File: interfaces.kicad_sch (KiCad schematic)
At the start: 36 parts, among them J4 1140084168, J5 0473460001, U1 TS3USB30EDGSR, U5 TS3USB30EDGSR, U6 FT234XD-R

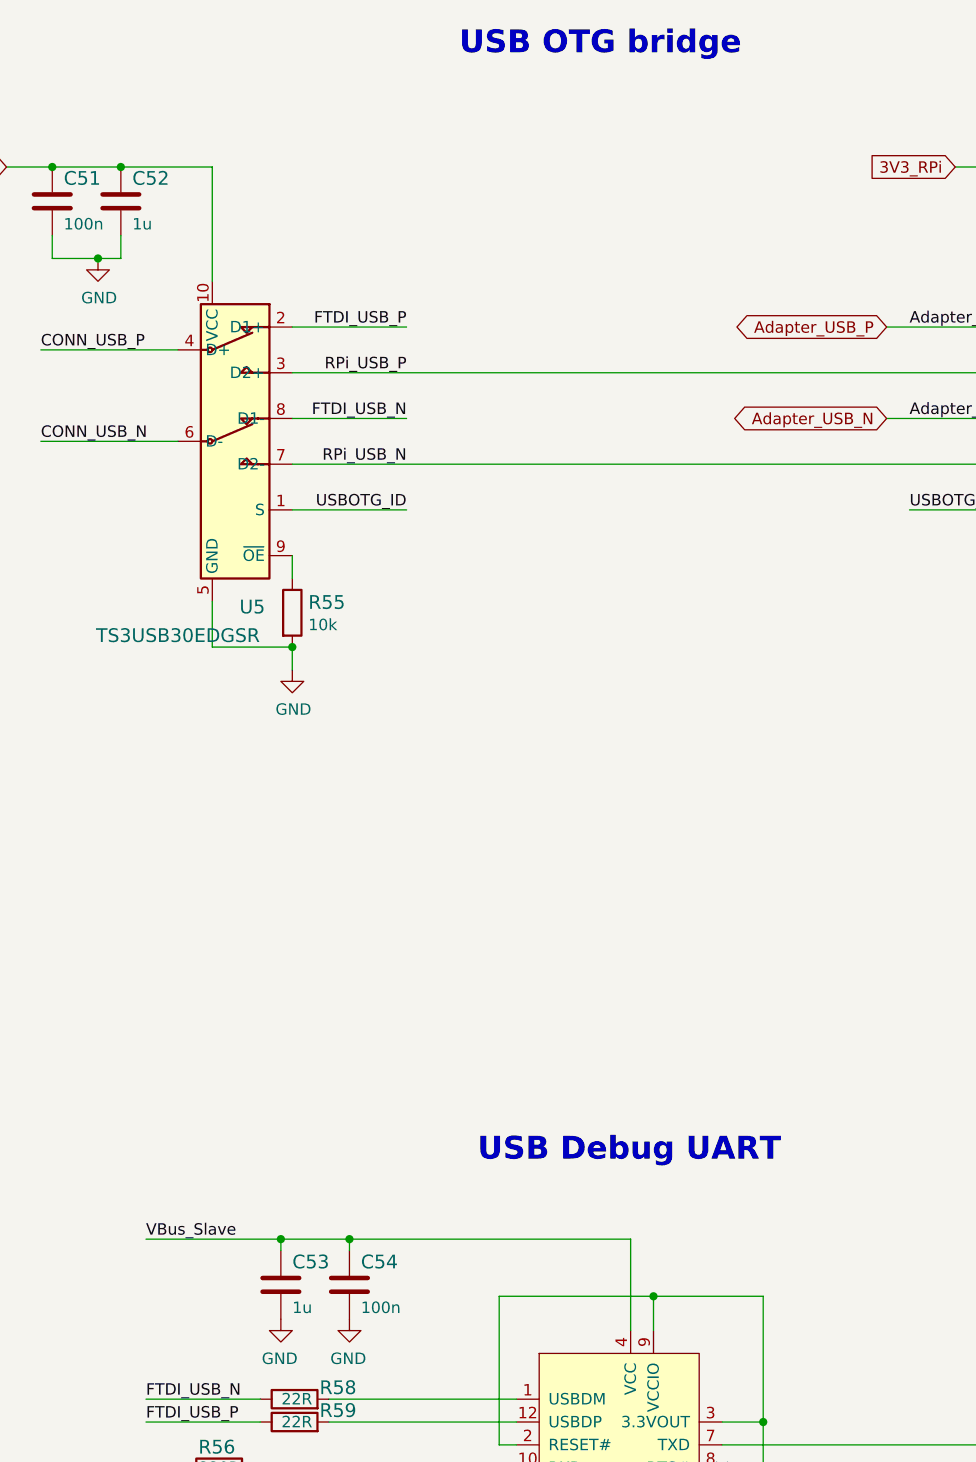
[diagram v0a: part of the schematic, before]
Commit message: Update C1,C2,C3 symbol and footprint
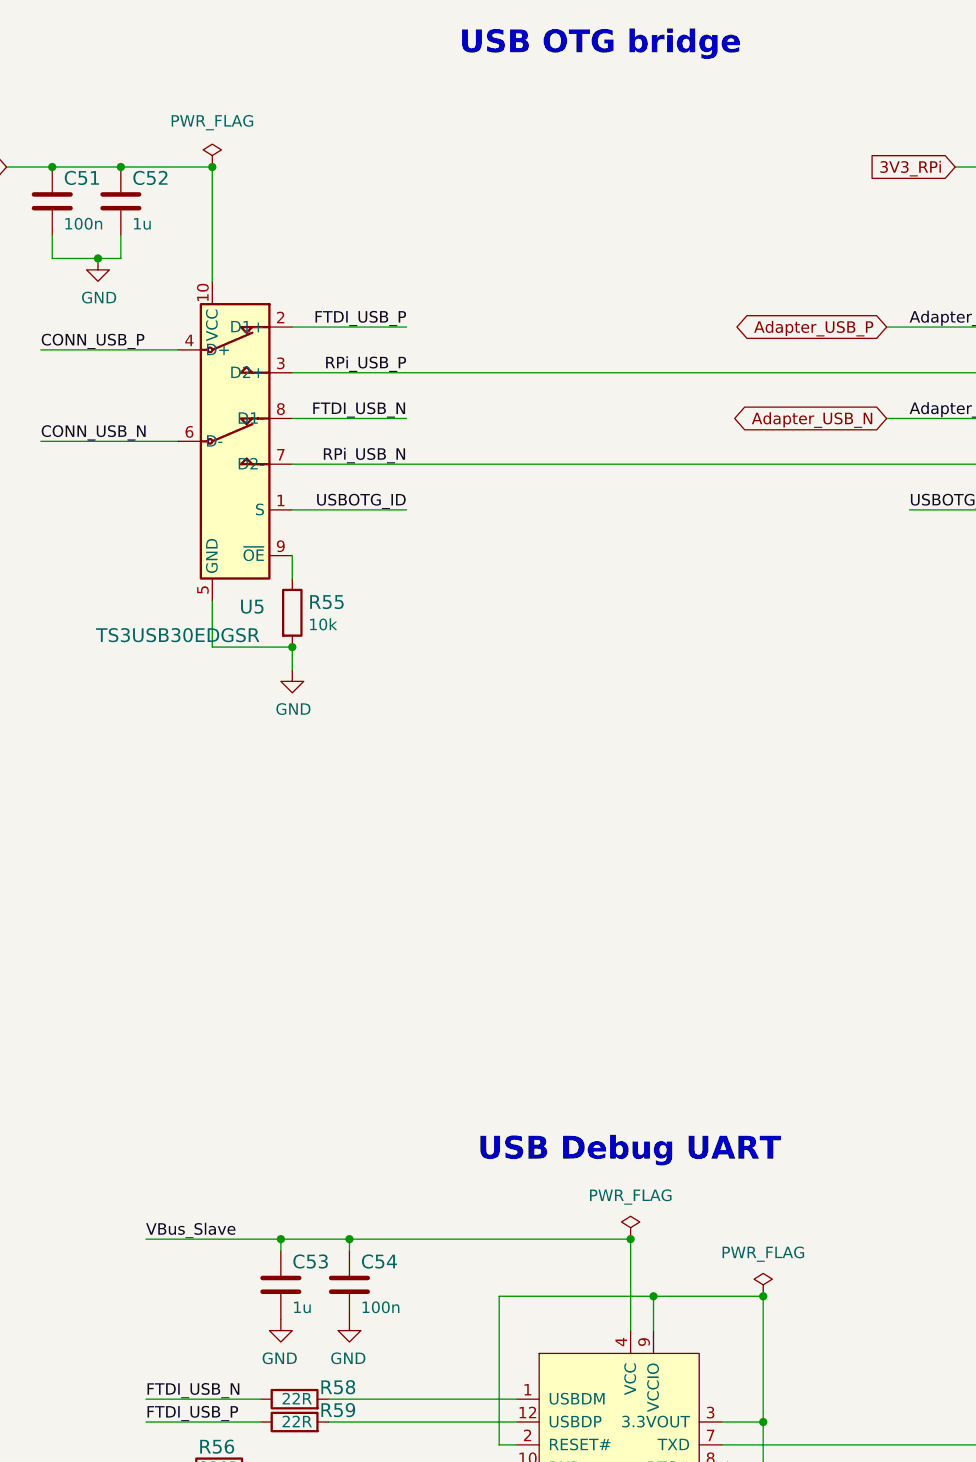
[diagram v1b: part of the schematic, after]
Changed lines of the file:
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@@
   (junction (at 45.466 188.976) (diameter 0) (color 0 0 0 0)
   )
+  (junction (at 232.41 48.26) (diameter 0) (color 0 0 0 0)
+  )
   (junction (at 50.546 178.816) (diameter 0) (color 0 0 0 0)
   )
@@
   (junction (at 111.506 205.486) (diameter 0) (color 0 0 0 0)
   )
+  (junction (at 293.624 173.736) (diameter 0) (color 0 0 0 0)
+  )
   (junction (at 79.756 63.5) (diameter 0) (color 0 0 0 0)
   )
@@
   (junction (at 281.432 173.736) (diameter 0) (color 0 0 0 0)
   )
+  (junction (at 278.892 167.386) (diameter 0) (color 0 0 0 0)
+  )
   (junction (at 74.676 188.976) (diameter 0) (color 0 0 0 0)
   )
@@
     (pin "2")
   )
+  (symbol (lib_id "antmicropower:PWR_FLAG") (at 293.624 173.736 0) (unit 1)
+    (in_bom yes) (on_board yes) (fields_autoplaced)
+    (property "Reference" "#FLG0103" (id 0) (at 293.624 171.831 0)
+      (effects (font (size 1.27 1.27)) hide)
+    )
+    (property "Value" "PWR_FLAG" (id 1) (at 293.624 168.91 0))
+    (property "Footprint" "" (id 2) (at 293.624 173.736 0)
+      (effects (font (size 1.27 1.27)) hide)
+    )
+    (property "Datasheet" "" (id 3) (at 293.624 173.736 0)
+      (effects (font (size 1.27 1.27)) hide)
+    )
+    (pin "1")
+  )
+  (symbol (lib_id "antmicropower:PWR_FLAG") (at 278.892 167.386 0) (unit 1)
+    (in_bom yes) (on_board yes) (fields_autoplaced)
+    (property "Reference" "#FLG0104" (id 0) (at 278.892 165.481 0)
+      (effects (font (size 1.27 1.27)) hide)
+    )
+    (property "Value" "PWR_FLAG" (id 1) (at 278.892 162.56 0))
+    (property "Footprint" "" (id 2) (at 278.892 167.386 0)
+      (effects (font (size 1.27 1.27)) hide)
+    )
+    (property "Datasheet" "" (id 3) (at 278.892 167.386 0)
+      (effects (font (size 1.27 1.27)) hide)
+    )
+    (pin "1")
+  )
+  (symbol (lib_id "antmicropower:PWR_FLAG") (at 232.41 48.26 0) (unit 1)
+    (in_bom yes) (on_board yes) (fields_autoplaced)
+    (property "Reference" "#FLG0102" (id 0) (at 232.41 46.355 0)
+      (effects (font (size 1.27 1.27)) hide)
+    )
+    (property "Value" "PWR_FLAG" (id 1) (at 232.41 43.18 0))
+    (property "Footprint" "" (id 2) (at 232.41 48.26 0)
+      (effects (font (size 1.27 1.27)) hide)
+    )
+    (property "Datasheet" "" (id 3) (at 232.41 48.26 0)
+      (effects (font (size 1.27 1.27)) hide)
+    )
+    (pin "1")
+  )
 )

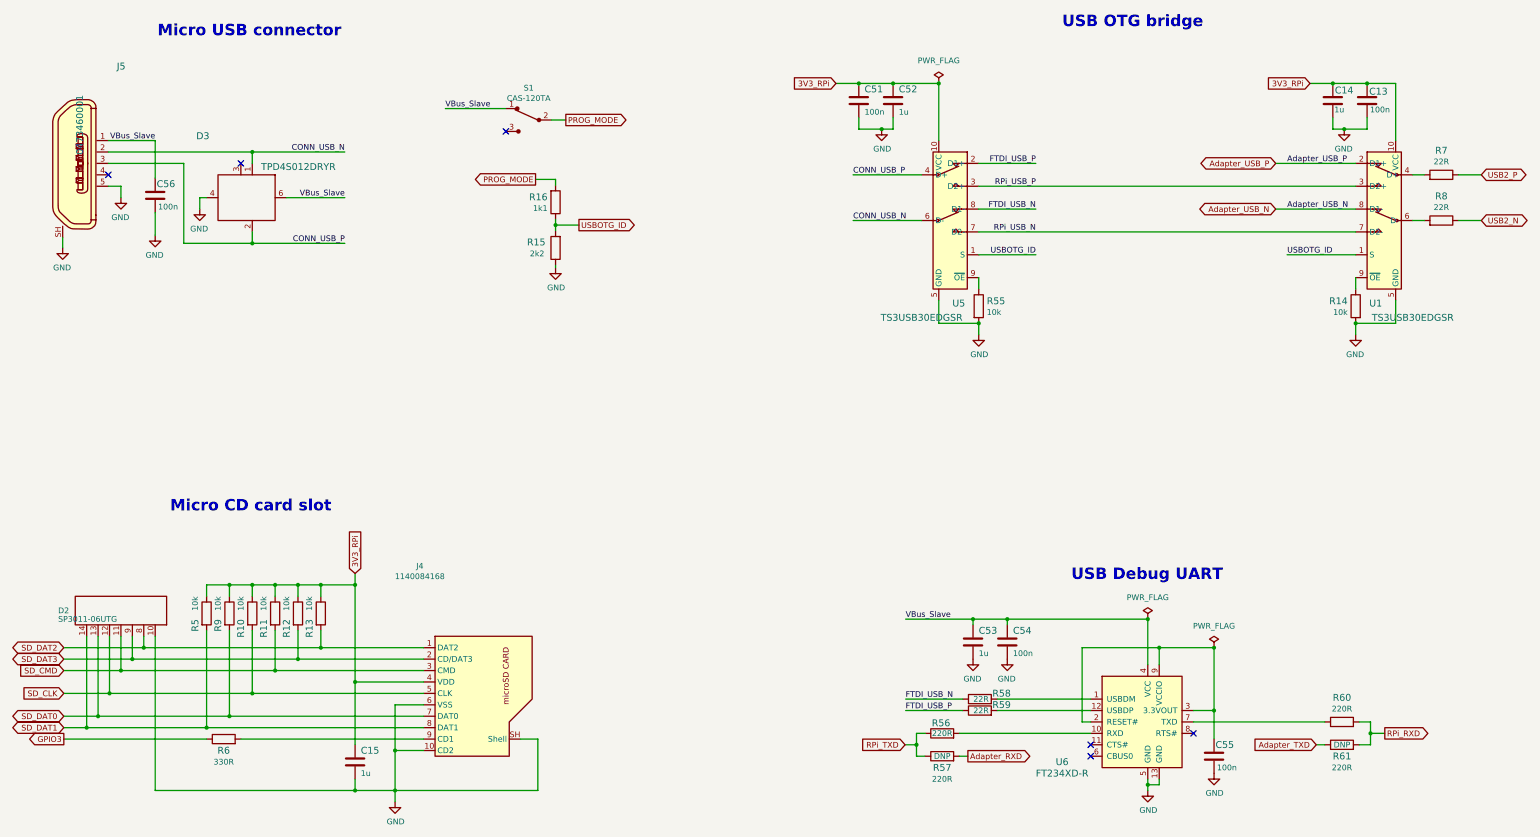
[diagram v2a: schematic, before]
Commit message: Update C13, C17, C21, C37, C51, C54, C55, C56 symbol and footprint
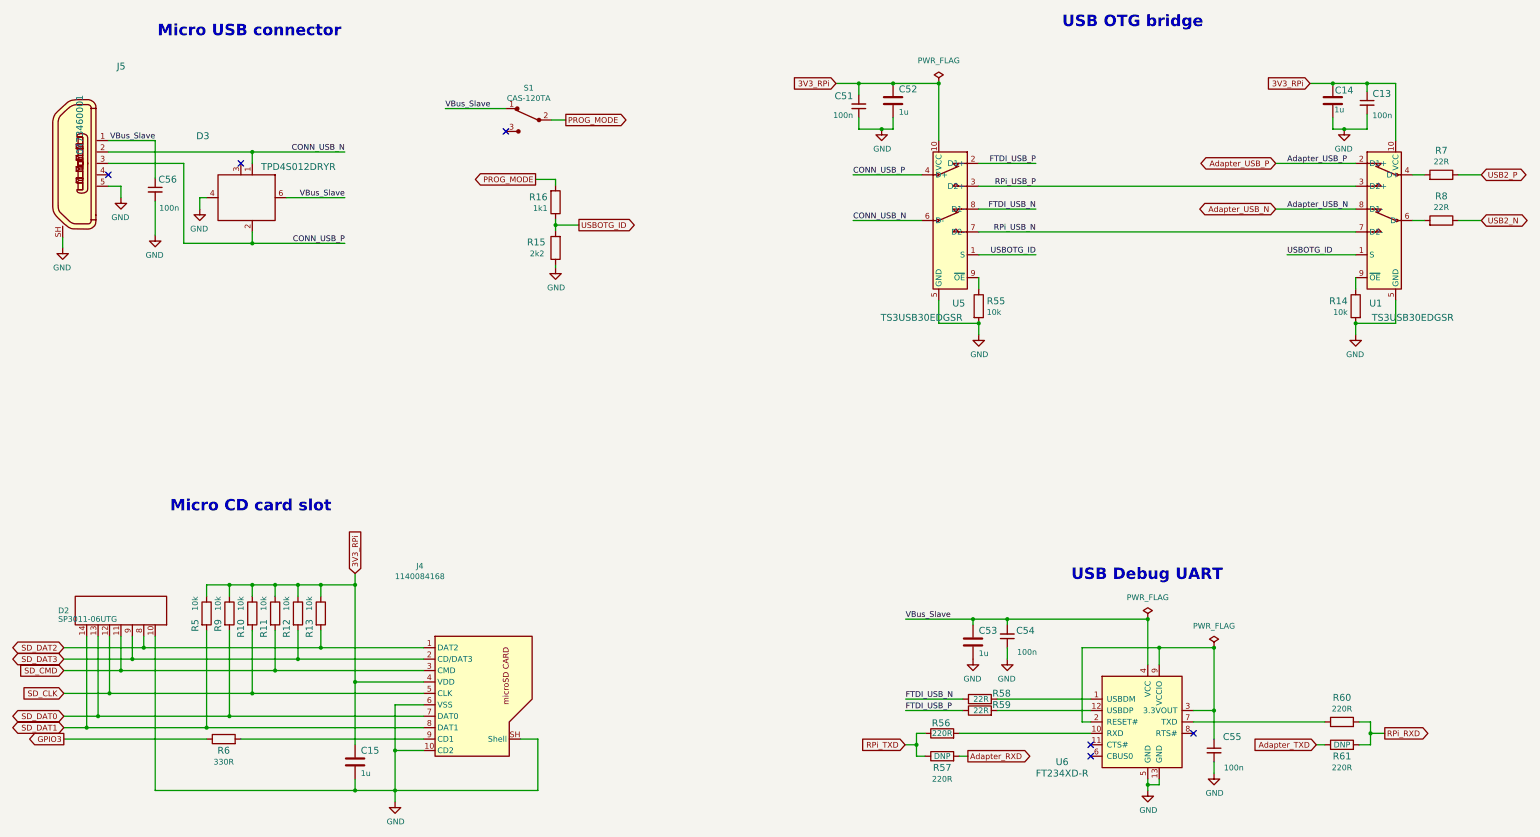
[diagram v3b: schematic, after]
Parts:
- C13, C51, C54, C55, C56: footprint scalenode-cm4-baseboard-footprints:0402-cap -> antmicro-footprints:C_0402_1005Metric; symbol scalenode-cm4-baseboard:C_100n_0402 -> antmicroCapacitors0402:C_100n_0402; Author (none) -> Antmicro; Dielectric (none) -> X5R; License (none) -> Apache-2.0; MPN 0402X104K6R3CT -> GRM155R61H104KE14D; Manufacturer Walsin -> Murata; Voltage (none) -> 50V
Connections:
- net 3V3_RPi: now also C51.2; no longer C51.1
- net GND: now also C51.1, C54.1; no longer C51.2, C54.2
- net VBus_Slave: now also C54.2; no longer C54.1
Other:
- moved on the sheet: C13, C51, C54, C55, C56

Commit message: Update C16, C18, C19 symbol and footprint
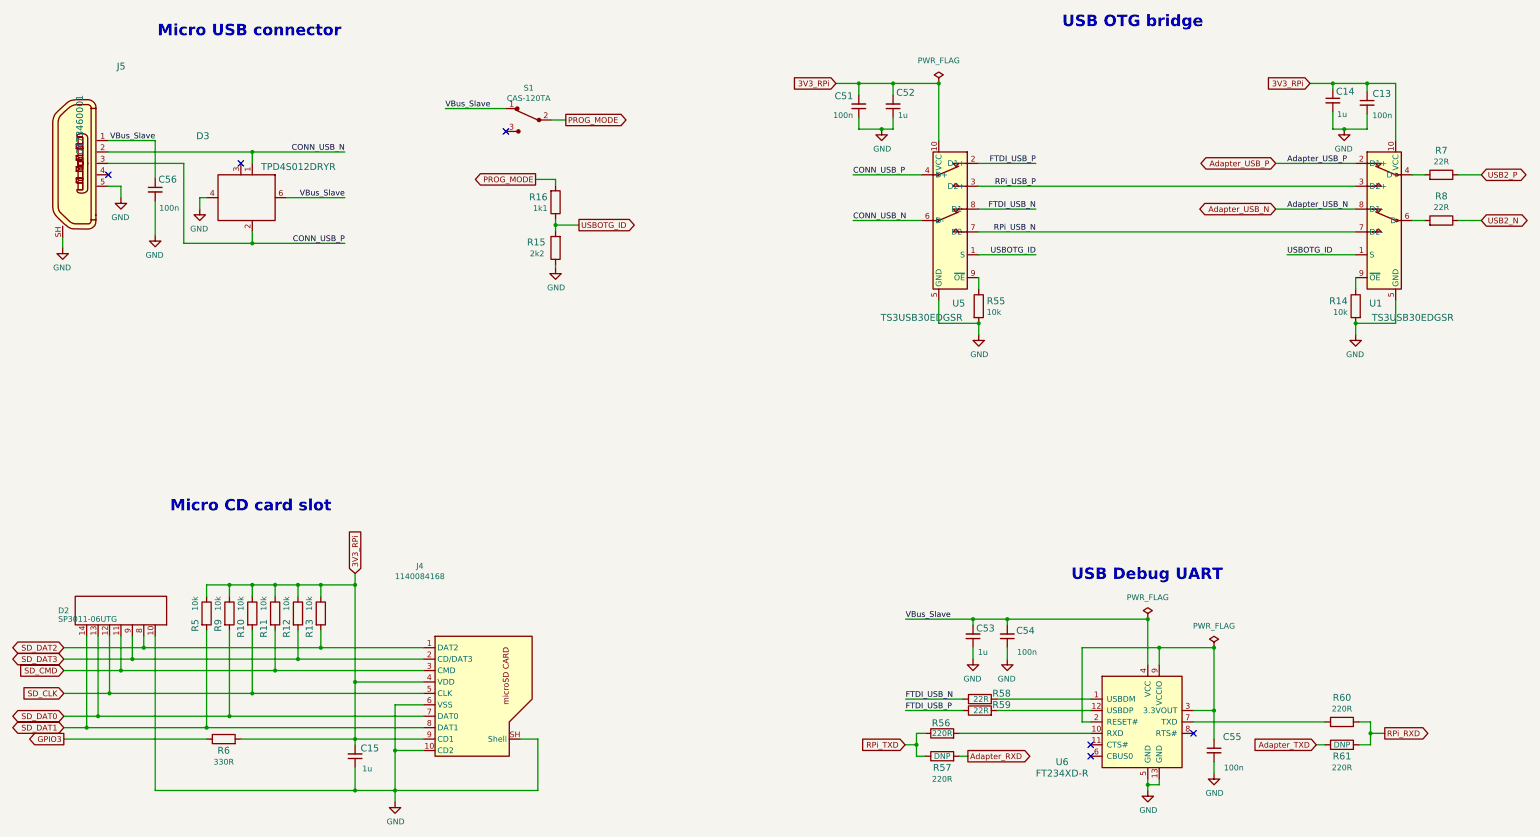
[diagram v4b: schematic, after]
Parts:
- C14, C15, C52, C53: footprint scalenode-cm4-baseboard-footprints:0402-cap -> antmicro-footprints:C_0402_1005Metric; symbol scalenode-cm4-baseboard:C_1u_0402 -> antmicroCapacitors0402:C_1u_0402; Author (none) -> Antmicro; License (none) -> Apache-2.0
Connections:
- net 3V3_RPi: now also C15.2, C52.2, J4.9 (CD1), R6.2; no longer C15.1, C52.1
- net GND: now also C15.1, C52.1, C53.1; no longer C15.2, C52.2, C53.2
- net VBus_Slave: now also C53.2; no longer C53.1
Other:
- moved on the sheet: C14, C15, C52, C53
